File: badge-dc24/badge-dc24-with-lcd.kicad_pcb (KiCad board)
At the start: 2 copper layers, 27 parts, among them U1 ESP-12E, U2 TSOP38238, U3 74HC595

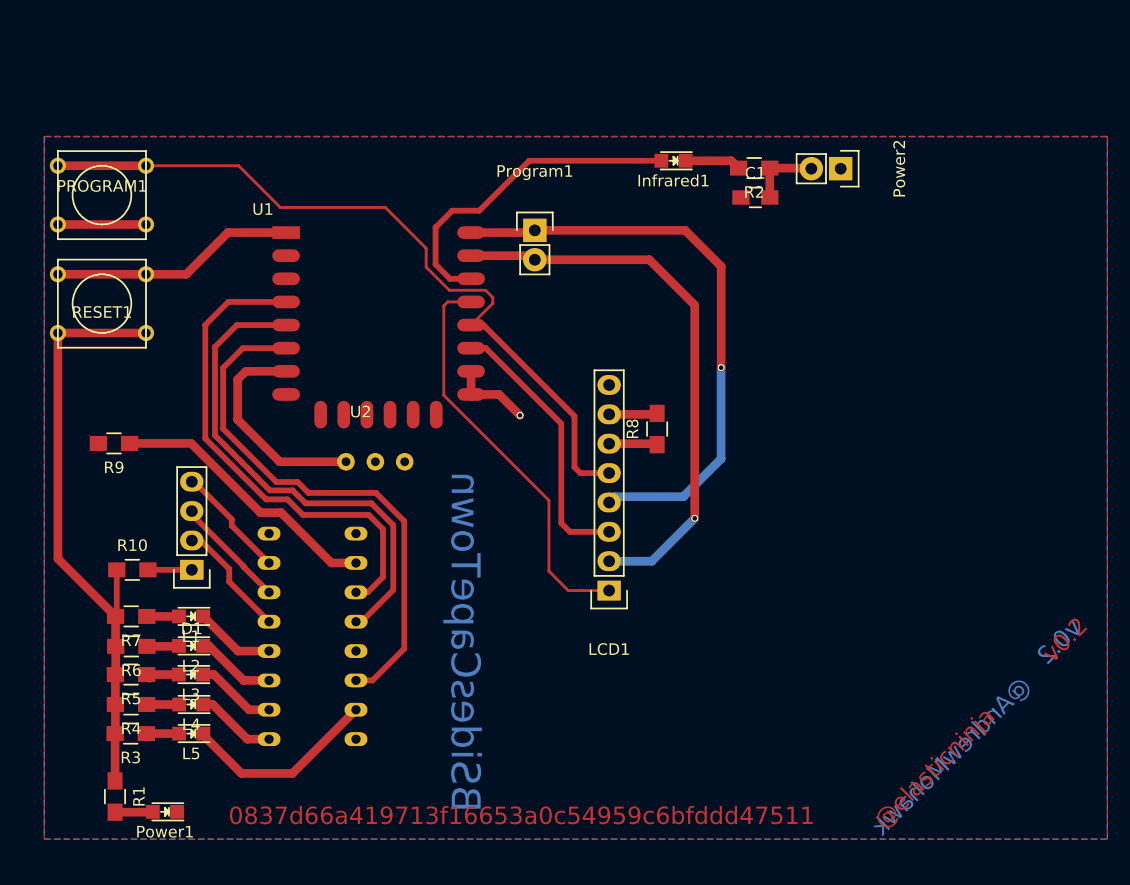
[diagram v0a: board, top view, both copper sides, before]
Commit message: LEDs to throughole
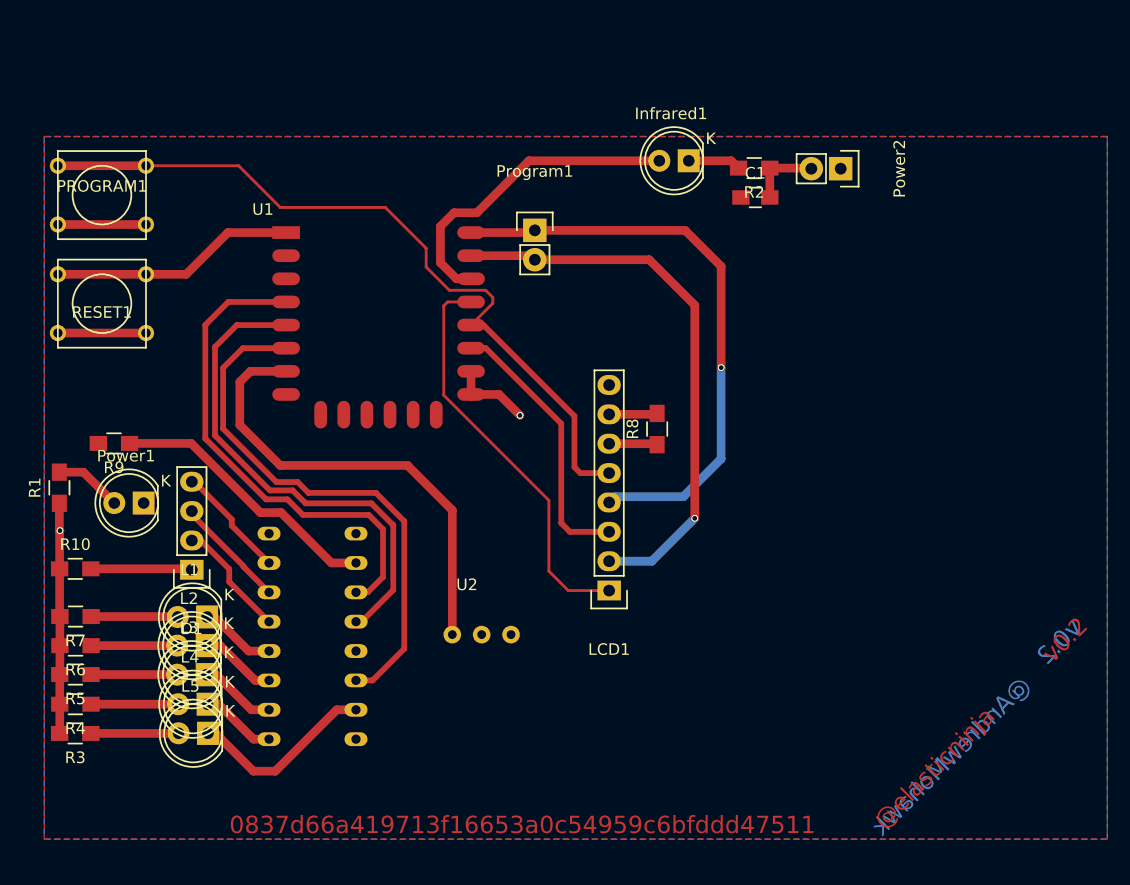
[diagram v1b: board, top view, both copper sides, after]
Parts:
- Infrared1: value LED -> LEDs:LED-5MM; footprint LEDs:LED_0805 -> LEDs:LED-5MM
- L1, L2, L3, L4, L5, Power1: footprint LEDs:LED_0805 -> LEDs:LED-5MM
- moved R1 27.1 mm to (56.1, 94.3), turned to 90 degrees
- moved Power1 26.8 mm to (63.4, 95.6)
- moved U2 17.5 mm to (91.4, 103.2)
- moved R10 4.94 mm to (57.5, 101.3)
- moved R6 4.83 mm to (57.5, 108.0)
- moved R4 4.81 mm to (57.5, 113.0)
- moved R7 4.81 mm to (57.5, 105.5)
- moved R5 4.81 mm to (57.5, 110.5)
- moved R3 4.80 mm to (57.5, 115.6)
- moved L5 1.45 mm to (69.0, 115.6)
- moved L4 1.41 mm to (68.9, 113.0)
- moved L1 1.39 mm to (68.9, 105.5)
- moved L3 1.36 mm to (68.8, 110.5)
- moved L2 1.35 mm to (68.8, 108.0)
- moved Infrared1 1.32 mm to (110.5, 66.0)
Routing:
- net GND: track 73.9 -> 48.9 mm, vias 1 -> 2
- net Net-(U1-Pad7): track 18.8 -> 40.3 mm
- net Net-(D1-Pad1): track 3.79 -> 8.77 mm
- net Net-(L5-Pad2): track 2.83 -> 7.60 mm
- net Net-(L4-Pad2): track 2.81 -> 7.54 mm
- net Net-(L1-Pad2): track 2.78 -> 7.50 mm
- net Net-(L2-Pad2): track 2.79 -> 7.45 mm
- net Net-(L3-Pad2): track 3.14 -> 7.47 mm
- net Net-(Power1-Pad2): track 3.28 -> 5.86 mm
- net Net-(Infrared1-Pad2): track 28.7 -> 27.7 mm
- net Net-(L5-Pad1): track 17.0 -> 16.4 mm
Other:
- board text removed: "BSidesCapeTown"

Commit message: LEDs
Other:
- board text added: "73950de5c7766f8ae4fb76bc7ecf4b83f05361bd"
- board text removed: "0837d66a419713f16653a0c54959c6bfddd47511"
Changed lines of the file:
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@@
     (links 61)
     (no_connects 0)
-    (area 0 0 0 0)
+    (area 49.57 58.46 152.36 130.77)
     (thickness 1.6)
     (drawings 9)
@@
     (effects (font (size 1.5 1.5) (thickness 0.3)))
   )
-  (gr_text 0837d66a419713f16653a0c54959c6bfddd47511 (at 96.1644 123.4948) (layer F.Cu)
+  (gr_text 73950de5c7766f8ae4fb76bc7ecf4b83f05361bd (at 96.1644 123.4948) (layer F.Cu)
     (effects (font (size 1.5 1.5) (thickness 0.3)))
   )

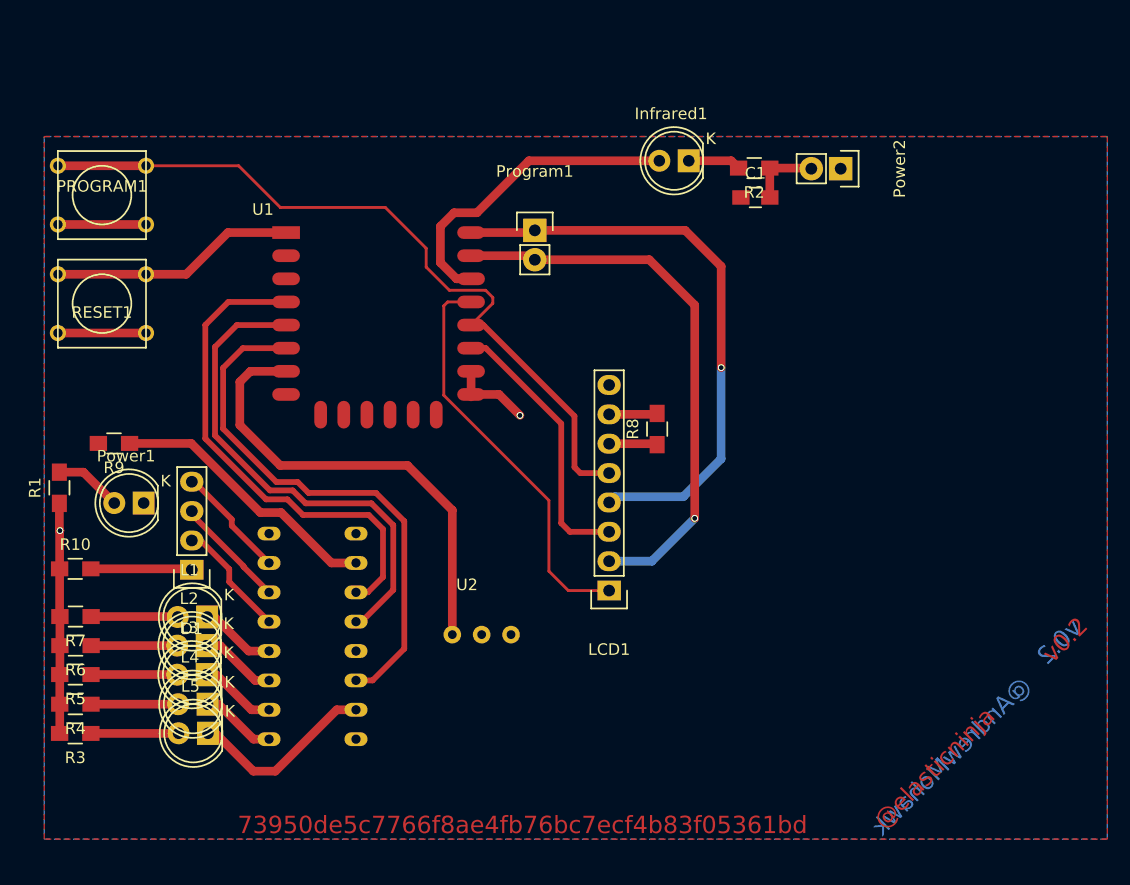
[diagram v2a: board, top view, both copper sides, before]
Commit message: More SMD components
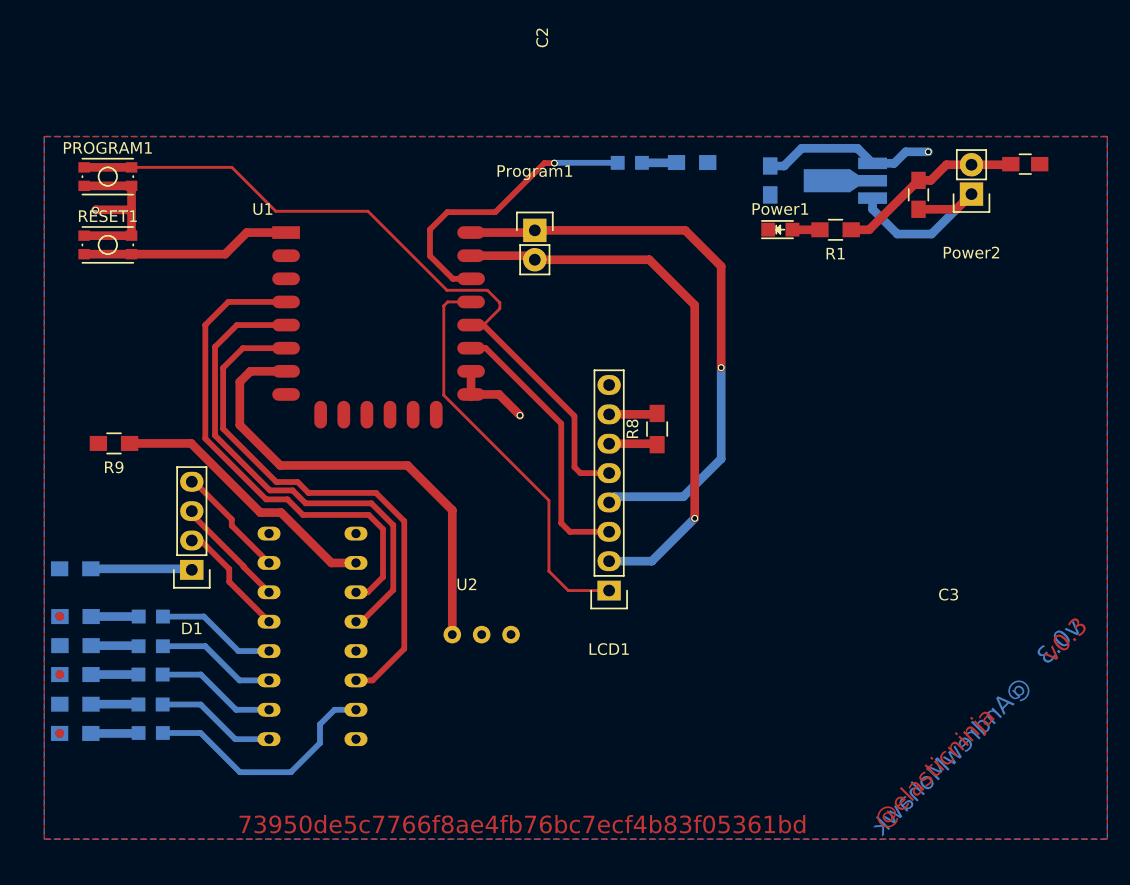
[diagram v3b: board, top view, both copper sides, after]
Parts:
- added C2: 1uF, Capacitors_SMD:C_0805_HandSoldering, F.Cu at (130.4, 69.0)
- added C3: 1uF, Capacitors_SMD:C_0805_HandSoldering, F.Cu at (139.6, 66.3)
- added U4: MC78L05ACH, TO_SOT_Packages_SMD:SOT89-3_Housing_Handsoldering, B.Cu at (124.1, 67.8)
- C1, R10, R2, R3, R4, R5, R6, R7: moved to B.Cu
- Infrared1, L1, L2, L3, L4, L5: footprint LEDs:LED-5MM -> LEDs:LED_0805; moved to B.Cu
- PROGRAM1, RESET1: footprint Buttons_Switches_ThroughHole:SW_PUSH_SMALL -> Buttons_Switches_SMD:SW_SPST_KMR2
- Power1: footprint LEDs:LED-5MM -> LEDs:LED_0805
- moved R1 70.7 mm to (123.2, 72.0), turned to 180 degrees
- moved Power1 59.9 mm to (118.5, 72.0), turned to 0 degrees
- moved Power2 11.5 mm to (135.0, 68.9), turned to 180 degrees
- moved R2 5.39 mm to (110.8, 66.2)
- moved RESET1 5.11 mm to (60.3, 73.3), turned to 0 degrees
- moved Infrared1 5.10 mm to (105.4, 66.2)
- moved L5 4.95 mm to (64.0, 115.5)
- moved L4 4.93 mm to (64.0, 113.1)
- moved L1 4.86 mm to (64.0, 105.5)
- moved L3 4.85 mm to (64.0, 110.5)
- moved L2 4.84 mm to (64.0, 108.0)
- moved C1 1.95 mm to (117.6, 67.7), turned to 270 degrees
- moved PROGRAM1 1.68 mm to (60.3, 67.4)
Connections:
- Power2 pad 1: +3V3 -> Net-(C2-Pad1)
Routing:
- net Net-(C2-Pad1): track 0.00 -> 17.0 mm
- net +3V3: track 4.19 -> 19.5 mm, vias 0 -> 1
- net GND: track 48.9 -> 39.0 mm
- net Net-(L5-Pad1): track 16.4 -> 21.3 mm
- net Net-(L4-Pad1): track 6.57 -> 10.4 mm
- net Net-(L1-Pad1): track 6.58 -> 10.4 mm
- net Net-(L3-Pad1): track 6.65 -> 10.5 mm
- net Net-(L2-Pad1): track 6.64 -> 10.4 mm
- net Net-(Power1-Pad2): track 5.86 -> 2.38 mm
- net Net-(L5-Pad2): track 7.60 -> 4.14 mm
- net Net-(L4-Pad2): track 7.54 -> 4.11 mm
- net Net-(L1-Pad2): track 7.50 -> 4.12 mm
- net Net-(L3-Pad2): track 7.47 -> 4.10 mm
- net Net-(L2-Pad2): track 7.45 -> 4.12 mm
- net Net-(RESET1-Pad2): track 21.2 -> 18.2 mm
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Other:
- board text added: "v0.3"
- board text removed: "v0.2"

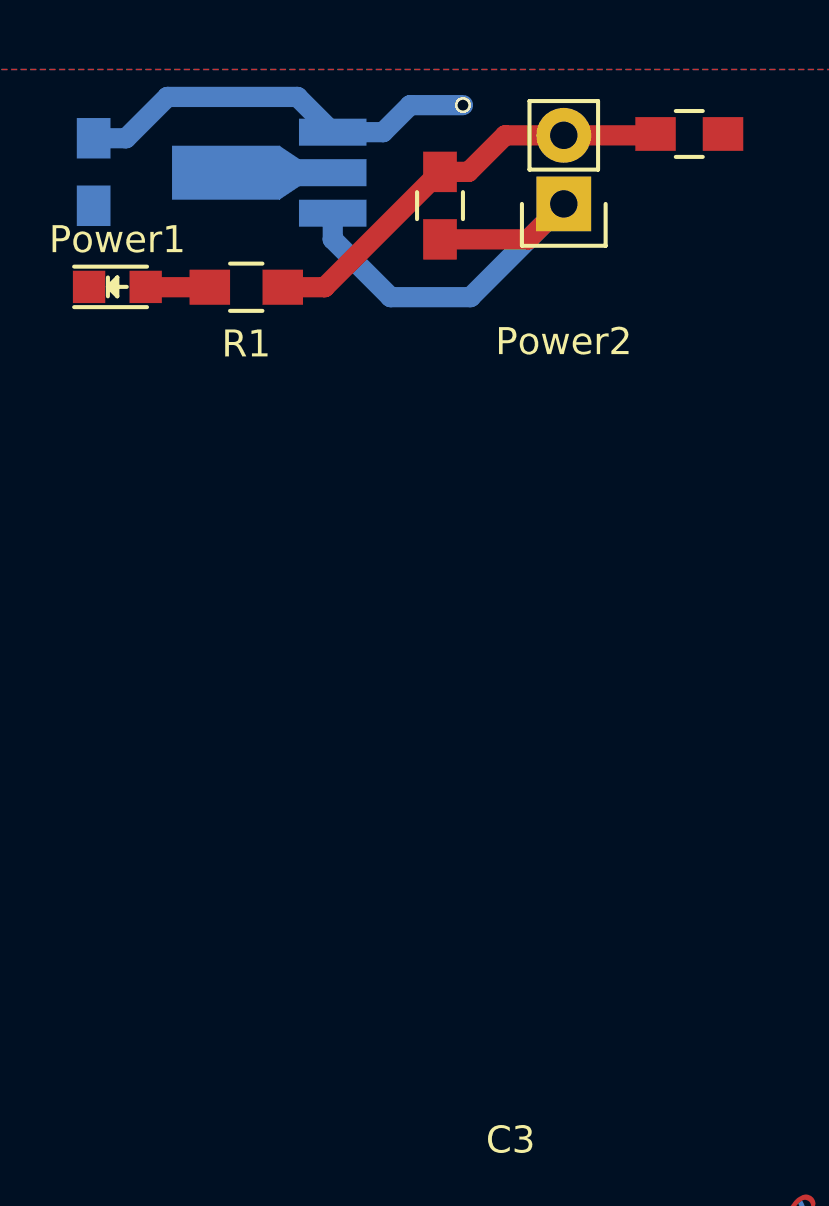
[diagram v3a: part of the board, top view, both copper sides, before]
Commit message: v0.3 with SMD
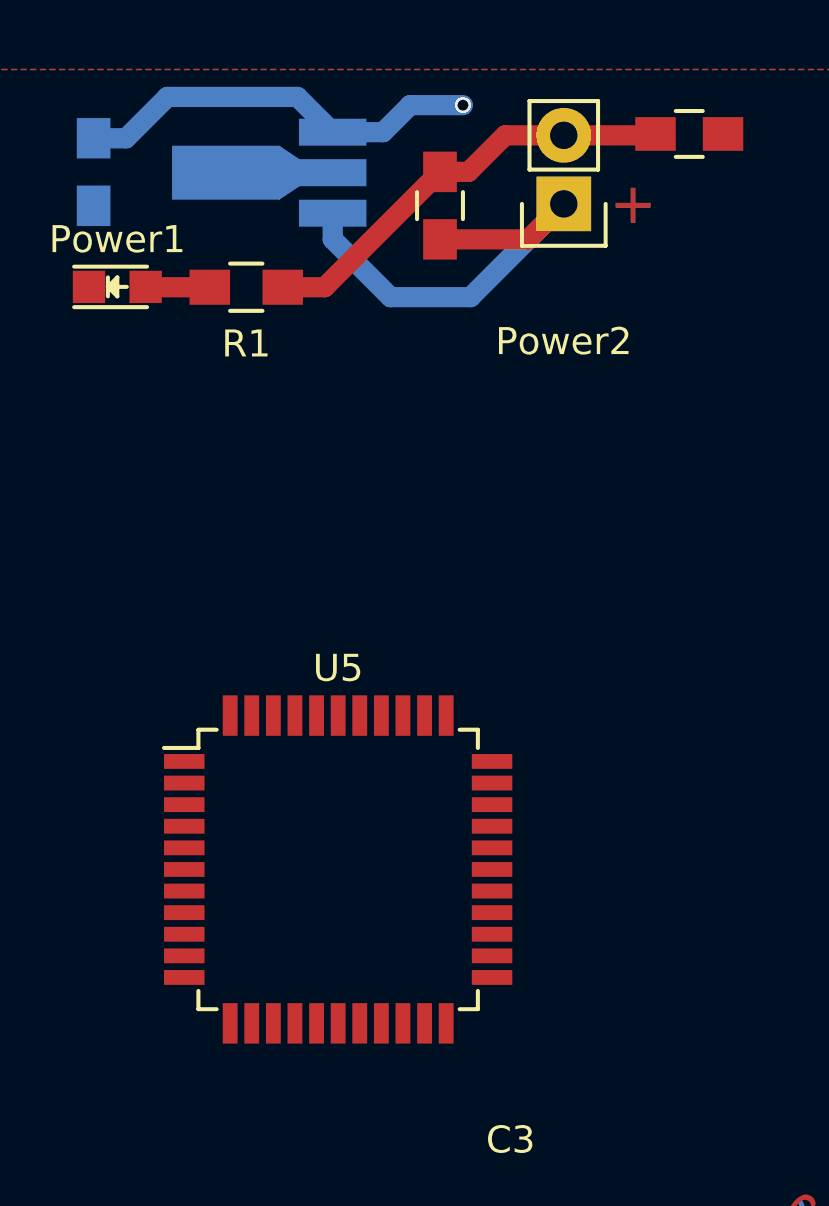
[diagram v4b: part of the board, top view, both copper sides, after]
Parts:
- added U5: ATMEGA32U4-M, Housings_QFP:TQFP-44_10x10mm_Pitch0.8mm, F.Cu at (126.6, 93.6)
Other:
- board text added: "+"
